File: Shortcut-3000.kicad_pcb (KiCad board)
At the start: 2 copper layers, 45 parts, among them J1 MagneticPogo_1x05_Female, J10 MagneticPogo_1x05_Female, J11 MagneticPogo_1x05_Female, J12 MagneticPogo_1x05_Female, J2 MagneticPogo_1x05_Female, J3 MagneticPogo_1x05_Female, J4 MagneticPogo_1x05_Female, J5 MagneticPogo_1x05_Female, J6 MagneticPogo_1x05_Female, J7 MagneticPogo_1x05_Female, J8 MagneticPogo_1x05_Female, J9 MagneticPogo_1x05_Female, SW1 SW_Push, SW10 SW_Push, SW11 SW_Push, SW12 SW_Push, SW13 SW_Push, SW14 SW_Push, SW15 SW_Push, SW16 RotaryEncoder_Switch, SW17 RotaryEncoder_Switch, SW2 SW_Push, SW3 SW_Push, SW4 SW_Push, SW5 SW_Push, SW6 SW_Push, SW7 SW_Push, SW8 SW_Push, SW9 SW_Push

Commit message: Switch to RP2040-Zero and route connectors through TCA9548A muxes
- Add Waveshare RP2040-Zero symbol and castellated footprint to the
  project library (dimensions from Waveshare's drawing) and replace the
  Raspberry Pi Pico with it
- Split the connectors across both I2C buses: J1-J6 on I2C0 (GP4/GP5),
  J7-J12 on I2C1 (GP6/GP7)
- Repurpose connector pin 5 as an open-drain INT line, shared per bus
  (INT0 = GP8, INT1 = GP9)
- Give each connector its own TCA9548A channel: J1-J6 on U1 ch 0-5,
  J7-J12 on U2 ch 0-5; channels 6-7 marked no-connect
- Ground mux pin 12, add 10k RESET pull-ups (R7-R8), 4.7k upstream
  pull-ups (R1-R4), 10k INT pull-ups (R5-R6) and 4.7k per-channel
  pull-ups (R9-R32)

Co-Authored-By: Claude Opus 5.5 <noreply@anthropic.com>
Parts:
- removed D1, D10, D11, D12, D13, D14, D15, D2, D3, D4, D5, D6, D7, D8, D9: 1N4148, Diode_THT:D_DO-35_SOD27_P7.62mm_Horizontal
- removed SW1, SW10, SW11, SW12, SW13, SW14, SW15, SW2, SW3, SW4, SW5, SW6, SW7, SW8, SW9: SW_Push, PCM_marbastlib-mx:SW_MX_HS_CPG151101S11_1u
- removed SW16, SW17: RotaryEncoder_Switch, Rotary_Encoder:RotaryEncoder_Alps_EC11E-Switch_Vertical_H20mm
- added R1: 4.7k, Resistor_THT:R_Axial_DIN0207_L6.3mm_D2.5mm_P7.62mm_Horizontal, F.Cu at (19.1, 22.5)
- added R10: 4.7k, Resistor_THT:R_Axial_DIN0207_L6.3mm_D2.5mm_P7.62mm_Horizontal, F.Cu at (19.1, 59.0)
- added R11: 4.7k, Resistor_THT:R_Axial_DIN0207_L6.3mm_D2.5mm_P7.62mm_Horizontal, F.Cu at (19.1, 63.0)
- added R12: 4.7k, Resistor_THT:R_Axial_DIN0207_L6.3mm_D2.5mm_P7.62mm_Horizontal, F.Cu at (29.8, 22.5)
- added R13: 4.7k, Resistor_THT:R_Axial_DIN0207_L6.3mm_D2.5mm_P7.62mm_Horizontal, F.Cu at (29.8, 26.6)
- added R14: 4.7k, Resistor_THT:R_Axial_DIN0207_L6.3mm_D2.5mm_P7.62mm_Horizontal, F.Cu at (29.8, 30.6)
- added R15: 4.7k, Resistor_THT:R_Axial_DIN0207_L6.3mm_D2.5mm_P7.62mm_Horizontal, F.Cu at (29.8, 34.7)
- added R16: 4.7k, Resistor_THT:R_Axial_DIN0207_L6.3mm_D2.5mm_P7.62mm_Horizontal, F.Cu at (29.8, 38.7)
- added R17: 4.7k, Resistor_THT:R_Axial_DIN0207_L6.3mm_D2.5mm_P7.62mm_Horizontal, F.Cu at (29.8, 42.8)
- added R18: 4.7k, Resistor_THT:R_Axial_DIN0207_L6.3mm_D2.5mm_P7.62mm_Horizontal, F.Cu at (29.8, 46.8)
- added R19: 4.7k, Resistor_THT:R_Axial_DIN0207_L6.3mm_D2.5mm_P7.62mm_Horizontal, F.Cu at (29.8, 50.9)
- added R2: 4.7k, Resistor_THT:R_Axial_DIN0207_L6.3mm_D2.5mm_P7.62mm_Horizontal, F.Cu at (19.1, 26.6)
- added R20: 4.7k, Resistor_THT:R_Axial_DIN0207_L6.3mm_D2.5mm_P7.62mm_Horizontal, F.Cu at (29.8, 54.9)
- added R21: 4.7k, Resistor_THT:R_Axial_DIN0207_L6.3mm_D2.5mm_P7.62mm_Horizontal, F.Cu at (29.8, 59.0)
- added R22: 4.7k, Resistor_THT:R_Axial_DIN0207_L6.3mm_D2.5mm_P7.62mm_Horizontal, F.Cu at (29.8, 63.0)
- added R23: 4.7k, Resistor_THT:R_Axial_DIN0207_L6.3mm_D2.5mm_P7.62mm_Horizontal, F.Cu at (40.6, 22.5)
- added R24: 4.7k, Resistor_THT:R_Axial_DIN0207_L6.3mm_D2.5mm_P7.62mm_Horizontal, F.Cu at (40.6, 26.6)
- added R25: 4.7k, Resistor_THT:R_Axial_DIN0207_L6.3mm_D2.5mm_P7.62mm_Horizontal, F.Cu at (40.6, 30.6)
- added R26: 4.7k, Resistor_THT:R_Axial_DIN0207_L6.3mm_D2.5mm_P7.62mm_Horizontal, F.Cu at (40.6, 34.7)
- added R27: 4.7k, Resistor_THT:R_Axial_DIN0207_L6.3mm_D2.5mm_P7.62mm_Horizontal, F.Cu at (40.6, 38.7)
- added R28: 4.7k, Resistor_THT:R_Axial_DIN0207_L6.3mm_D2.5mm_P7.62mm_Horizontal, F.Cu at (40.6, 42.8)
- added R29: 4.7k, Resistor_THT:R_Axial_DIN0207_L6.3mm_D2.5mm_P7.62mm_Horizontal, F.Cu at (40.6, 46.8)
- added R3: 4.7k, Resistor_THT:R_Axial_DIN0207_L6.3mm_D2.5mm_P7.62mm_Horizontal, F.Cu at (19.1, 30.6)
- added R30: 4.7k, Resistor_THT:R_Axial_DIN0207_L6.3mm_D2.5mm_P7.62mm_Horizontal, F.Cu at (40.6, 50.9)
- added R31: 4.7k, Resistor_THT:R_Axial_DIN0207_L6.3mm_D2.5mm_P7.62mm_Horizontal, F.Cu at (40.6, 54.9)
- added R32: 4.7k, Resistor_THT:R_Axial_DIN0207_L6.3mm_D2.5mm_P7.62mm_Horizontal, F.Cu at (40.6, 59.0)
- added R4: 4.7k, Resistor_THT:R_Axial_DIN0207_L6.3mm_D2.5mm_P7.62mm_Horizontal, F.Cu at (19.1, 34.7)
- added R5: 10k, Resistor_THT:R_Axial_DIN0207_L6.3mm_D2.5mm_P7.62mm_Horizontal, F.Cu at (19.1, 38.7)
- added R6: 10k, Resistor_THT:R_Axial_DIN0207_L6.3mm_D2.5mm_P7.62mm_Horizontal, F.Cu at (19.1, 42.8)
- added R7: 10k, Resistor_THT:R_Axial_DIN0207_L6.3mm_D2.5mm_P7.62mm_Horizontal, F.Cu at (19.1, 46.8)
- added R8: 10k, Resistor_THT:R_Axial_DIN0207_L6.3mm_D2.5mm_P7.62mm_Horizontal, F.Cu at (19.1, 50.9)
- added R9: 4.7k, Resistor_THT:R_Axial_DIN0207_L6.3mm_D2.5mm_P7.62mm_Horizontal, F.Cu at (19.1, 54.9)
- added U1: TCA9548APWR, Package_SO:TSSOP-24_4.4x7.8mm_P0.65mm, F.Cu at (54.6, 52.4)
- added U2: TCA9548APWR, Package_SO:TSSOP-24_4.4x7.8mm_P0.65mm, F.Cu at (63.7, 52.4)
- A1: value RaspberryPi_Pico -> RP2040-Zero; footprint Module:RaspberryPi_Pico_Common_THT -> Shortcut-3000:RP2040-Zero_Castellated
- moved A1 175.9 mm to (61.9, 33.3)
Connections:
- A1 pad 1: /COL0 -> unconnected-(A1-5V-Pad1)
- A1 pad 10: /ROW2 -> unconnected-(A1-GP13-Pad10)
- A1 pad 11: /Rotary_1_A -> unconnected-(A1-GP12-Pad11)
- A1 pad 12: /Rotary_1_B -> unconnected-(A1-GP11-Pad12)
- A1 pad 13: GND -> unconnected-(A1-GP10-Pad13)
- A1 pad 14: /Rotary_2_A -> /INT1
- A1 pad 15: /Rotary_2_B -> /INT0
- A1 pad 16: /Rotary_1_Push -> /SCL1
- A1 pad 17: /Rotary_2_Push -> /SDA1
- A1 pad 18: GND -> /SCL0
- A1 pad 19: /SDA -> /SDA0
- A1 pad 2: /COL1 -> GND
- A1 pad 20: /SCL -> unconnected-(A1-GP3-Pad20)
- A1 pad 23: GND -> unconnected-(A1-GP0-Pad23)
- A1 pad 3: GND -> +3V3
- A1 pad 4: /COL2 -> unconnected-(A1-GP29-Pad4)
- A1 pad 5: /COL3 -> unconnected-(A1-GP28-Pad5)
- A1 pad 6: /COL4 -> unconnected-(A1-GP27-Pad6)
- A1 pad 7: /ROW0 -> unconnected-(A1-GP26-Pad7)
- A1 pad 8: GND -> unconnected-(A1-GP15-Pad8)
- A1 pad 9: /ROW1 -> unconnected-(A1-GP14-Pad9)
- J1 pad 2: /SCL -> /SCL_J1
- J1 pad 4: /SDA -> /SDA_J1
- J1 pad 5: GND -> /INT0
- J10 pad 2: /SCL -> /SCL_J10
- J10 pad 4: /SDA -> /SDA_J10
- J10 pad 5: GND -> /INT1
- J11 pad 2: /SCL -> /SCL_J11
- J11 pad 4: /SDA -> /SDA_J11
- J11 pad 5: GND -> /INT1
- J12 pad 2: /SCL -> /SCL_J12
- J12 pad 4: /SDA -> /SDA_J12
- J12 pad 5: GND -> /INT1
- J2 pad 2: /SCL -> /SCL_J2
- J2 pad 4: /SDA -> /SDA_J2
- J2 pad 5: GND -> /INT0
- J3 pad 2: /SCL -> /SCL_J3
- J3 pad 4: /SDA -> /SDA_J3
- J3 pad 5: GND -> /INT0
- J4 pad 2: /SCL -> /SCL_J4
- J4 pad 4: /SDA -> /SDA_J4
- J4 pad 5: GND -> /INT0
- J5 pad 2: /SCL -> /SCL_J5
- J5 pad 4: /SDA -> /SDA_J5
- J5 pad 5: GND -> /INT0
- J6 pad 2: /SCL -> /SCL_J6
- J6 pad 4: /SDA -> /SDA_J6
- J6 pad 5: GND -> /INT0
- J7 pad 2: /SCL -> /SCL_J7
- J7 pad 4: /SDA -> /SDA_J7
- J7 pad 5: GND -> /INT1
- J8 pad 2: /SCL -> /SCL_J8
- J8 pad 4: /SDA -> /SDA_J8
- J8 pad 5: GND -> /INT1
- J9 pad 2: /SCL -> /SCL_J9
- J9 pad 4: /SDA -> /SDA_J9
- J9 pad 5: GND -> /INT1

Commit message: Backup before removing PCB routing
Co-Authored-By: Claude Opus 5.5 <noreply@anthropic.com>
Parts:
- A1, U1, U2: moved to B.Cu
- R1, R10, R11, R12, R13, R14, R15, R16, R17, R18, R19, R2, R20, R21, R22, R23, R24, R25, R26, R27, R28, R29, R3, R30, R31, R32, R4, R5, R6, R7, R8, R9: footprint Resistor_THT:R_Axial_DIN0207_L6.3mm_D2.5mm_P7.62mm_Horizontal -> Resistor_SMD:R_0805_2012Metric; moved to B.Cu
- moved R8 158.6 mm to (176.3, 71.2), turned to -90 degrees
- moved R7 156.2 mm to (173.4, 71.2), turned to -90 degrees
- moved R6 154.0 mm to (170.4, 71.2), turned to -90 degrees
- moved J10 152.3 mm to (158.8, 102.7)
- moved J11 152.3 mm to (184.2, 102.7)
- moved J2 152.3 mm to (158.8, 51.9)
- moved J3 152.3 mm to (184.2, 51.9)
- moved J6 152.3 mm to (158.8, 77.3)
- moved J7 152.3 mm to (184.2, 77.3)
- moved J1 152.3 mm to (133.4, 51.9)
- moved J12 152.3 mm to (209.6, 102.7)
- moved J4 152.3 mm to (209.6, 51.9)
- moved J5 152.3 mm to (133.4, 77.3)
- moved J8 152.3 mm to (209.6, 77.3)
- moved J9 152.3 mm to (133.4, 102.7)
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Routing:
- net GND: track 0.00 -> 417.4 mm
- net +3V3: track 0.00 -> 405.8 mm, vias 0 -> 1
- net /INT1: track 0.00 -> 157.5 mm, vias 0 -> 3
- net /SCL_J12: track 0.00 -> 63.4 mm, vias 0 -> 1
- net /SCL_J11: track 0.00 -> 57.2 mm, vias 0 -> 1
- net /SDA_J12: track 0.00 -> 52.7 mm, vias 0 -> 1
- net /SDA_J11: track 0.00 -> 41.2 mm, vias 0 -> 1
- net /INT0: track 0.00 -> 38.6 mm
- net /SCL_J7: track 0.00 -> 32.6 mm, vias 0 -> 1
- net /SDA_J8: track 0.00 -> 30.6 mm
- net /SCL_J8: track 0.00 -> 26.9 mm
- net /SDA_J7: track 0.00 -> 22.7 mm, vias 0 -> 1
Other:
- board outline added: 105.5 x 82.5 mm

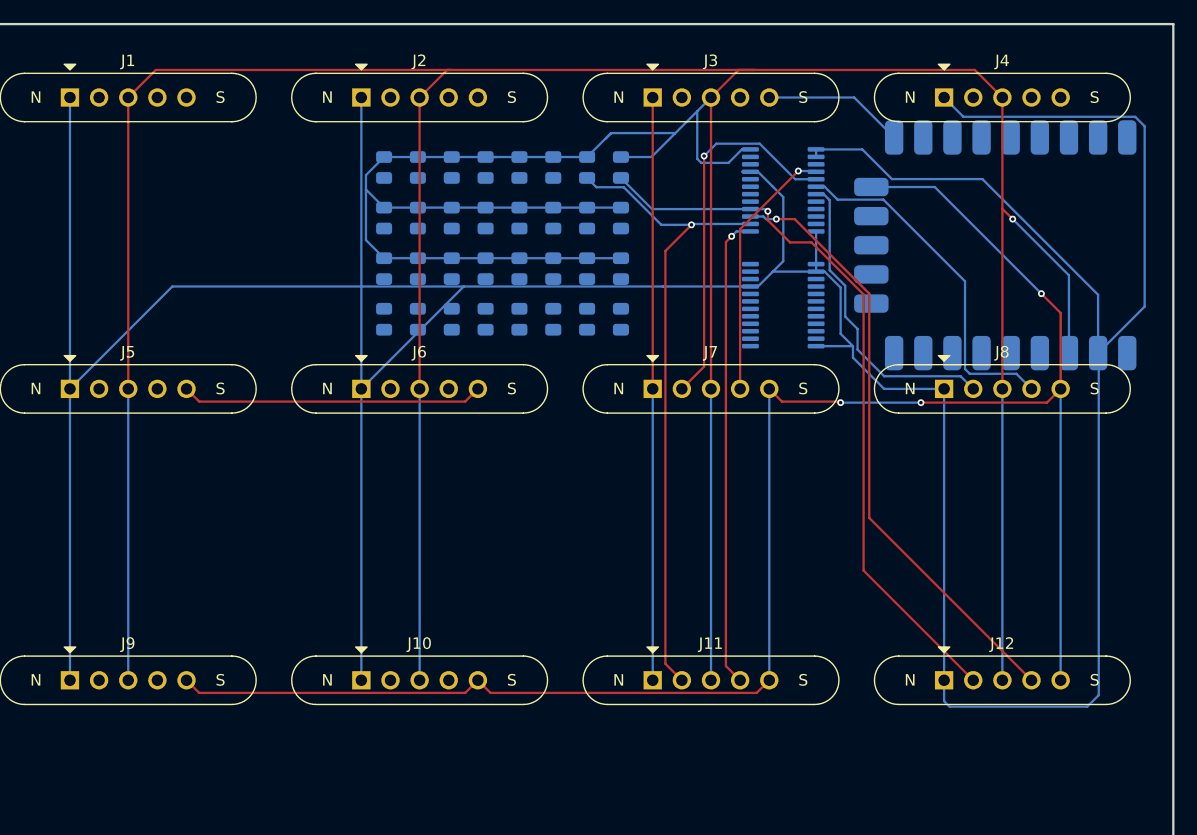
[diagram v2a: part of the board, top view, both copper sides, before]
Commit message: Backup before replacing 3V3 routing with fill
Co-Authored-By: Claude Opus 5.5 <noreply@anthropic.com>
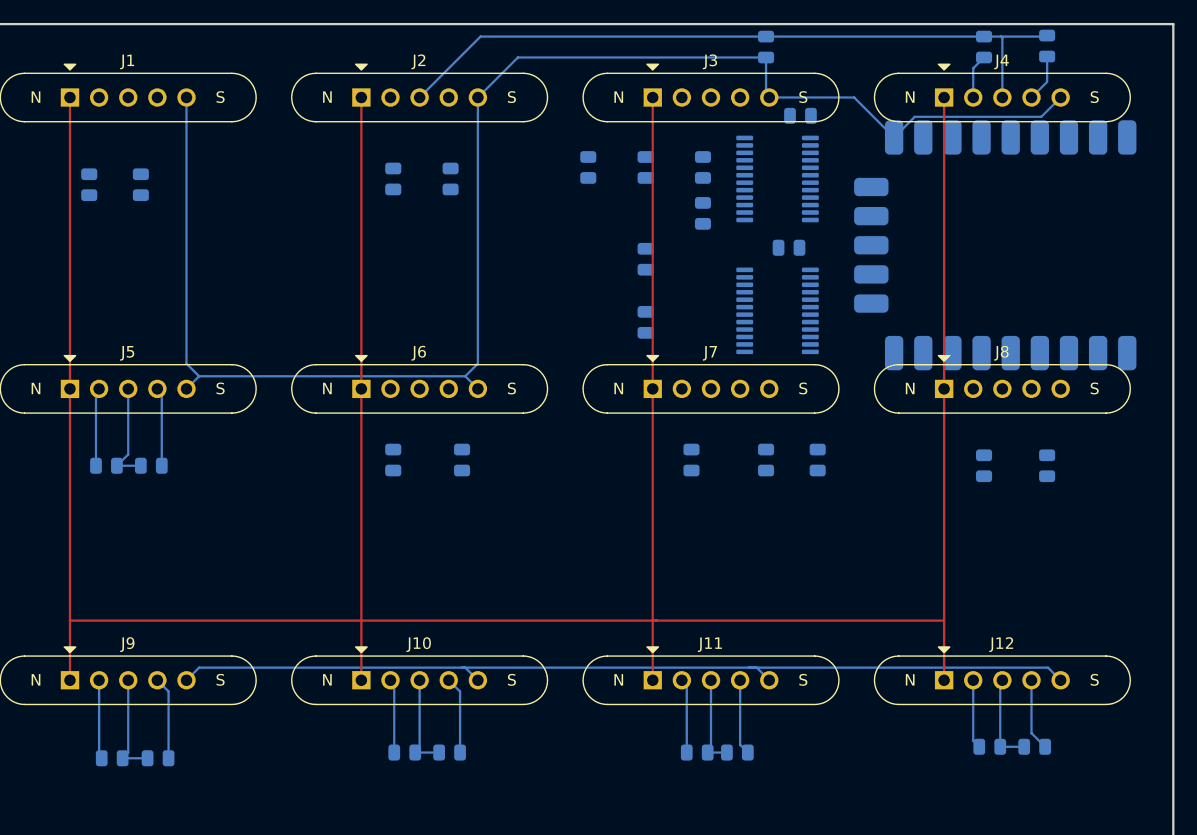
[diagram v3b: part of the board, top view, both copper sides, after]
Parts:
- moved R20 66.4 mm to (212.4, 108.5), turned to 0 degrees
- moved R29 62.5 mm to (132.0, 109.5), turned to 180 degrees
- moved R32 59.9 mm to (208.5, 108.5), turned to 180 degrees
- moved R19 52.8 mm to (186.5, 109.0), turned to 0 degrees
- moved R12 52.7 mm to (213.5, 47.4)
- moved R30 52.6 mm to (157.5, 109.0), turned to 180 degrees
- moved R31 51.9 mm to (183.0, 109.0), turned to 180 degrees
- moved R17 51.0 mm to (136.0, 109.5), turned to 0 degrees
- moved R28 50.6 mm to (208.0, 84.0)
- moved R18 46.7 mm to (161.4, 109.0), turned to 0 degrees
- moved R16 40.9 mm to (213.5, 84.0)
- moved R21 37.6 mm to (130.0, 59.5)
- moved R13 36.4 mm to (135.4, 84.0), turned to 0 degrees
- moved R25 35.5 mm to (131.5, 84.0), turned to 180 degrees
- moved R24 35.0 mm to (208.0, 47.5)
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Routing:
- net +3V3: track 405.8 -> 105.9 mm, vias 1 -> 0
- net GND: track 417.4 -> 279.8 mm
- net /INT0: track 38.6 -> 134.3 mm
- net /INT1: track 157.5 -> 81.2 mm, vias 3 -> 0
- net /SCL_J12: track 63.4 -> 6.02 mm, vias 1 -> 0
- net /SCL_J11: track 57.2 -> 6.48 mm, vias 1 -> 0
- net /SDA_J12: track 52.7 -> 6.29 mm, vias 1 -> 0
- net /SDA_J11: track 41.2 -> 6.58 mm, vias 1 -> 0
- net /SCL_J7: track 32.6 -> 0.00 mm, vias 1 -> 0
- net /SDA_J8: track 30.6 -> 0.00 mm
- net /SCL_J8: track 26.9 -> 0.00 mm
- net /SDA_J7: track 22.7 -> 0.00 mm, vias 1 -> 0
- net /SDA_J9: track 0.00 -> 7.20 mm
- net /SCL_J9: track 0.00 -> 6.89 mm
- net /SDA_J5: track 0.00 -> 6.86 mm
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
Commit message: Replace 3V3 routing with B.Cu 3V3 fill zone
Co-Authored-By: Claude Opus 5.5 <noreply@anthropic.com>
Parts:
- moved R11 10.3 mm to (173.5, 67.0), turned to 90 degrees
- moved U1 4.00 mm to (186.0, 70.5)
- moved R7 2.06 mm to (191.5, 67.0), turned to -90 degrees
- moved R12 1.50 mm to (213.5, 48.9)
- moved R24 1.50 mm to (208.0, 49.0)
- moved R1 1.00 mm to (178.5, 67.0)
- moved R2 1.00 mm to (178.5, 70.5)
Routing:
- net +3V3: track 105.9 -> 1.09 mm
- net /SCL_J1: track 0.00 -> 100.6 mm, vias 0 -> 1
- net /SDA_J1: track 0.00 -> 94.0 mm, vias 0 -> 1
- net /SCL_J2: track 0.00 -> 73.3 mm, vias 0 -> 1
- net /SDA_J3: track 0.00 -> 70.6 mm
- net /SCL_J5: track 6.81 -> 73.9 mm
- net /INT1: track 81.2 -> 145.9 mm
- net /SDA_J5: track 6.86 -> 69.7 mm, vias 0 -> 2
- net /SCL_J3: track 0.00 -> 47.7 mm
- net /SCL_J6: track 0.00 -> 45.7 mm, vias 0 -> 1
- net GND: track 279.8 -> 324.7 mm, vias 0 -> 2
- net /SDA_J4: track 4.14 -> 48.5 mm
- net /SDA_J2: track 0.00 -> 41.1 mm
- net /SDA_J6: track 0.00 -> 38.1 mm
- net /INT0: track 134.3 -> 172.3 mm
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- added copper zone on B.Cu, net +3V3

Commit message: Backup before changing pogo pin hole size
Co-Authored-By: Claude Opus 5.5 <noreply@anthropic.com>
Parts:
- moved R8 44.0 mm to (179.0, 95.5)
- moved R3 38.1 mm to (194.5, 94.5)
- moved U2 33.7 mm to (186.0, 92.4), turned to 0 degrees
- moved R4 30.5 mm to (194.5, 90.5)
- moved R2 1.50 mm to (177.0, 70.5)
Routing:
- net /SDA1: track 0.00 -> 84.4 mm, vias 0 -> 2
- net /SCL_J11: track 6.48 -> 88.7 mm
- net /SCL_J9: track 6.89 -> 64.1 mm
- net /SCL1: track 0.00 -> 54.3 mm, vias 0 -> 4
- net /SDA_J9: track 7.20 -> 59.1 mm
- net +3V3: track 1.09 -> 43.9 mm, vias 0 -> 8
- net /SDA_J12: track 6.29 -> 48.4 mm
- net /SDA0: track 4.78 -> 44.8 mm, vias 0 -> 2
- net /SDA_J8: track 8.18 -> 43.3 mm, vias 0 -> 2
- net /SCL_J10: track 6.44 -> 41.3 mm, vias 0 -> 1
- net /SCL_J8: track 8.05 -> 38.8 mm, vias 0 -> 2
- net /INT0: track 172.3 -> 143.2 mm, vias 0 -> 2
- net /SDA_J10: track 6.71 -> 35.6 mm, vias 0 -> 1
- net /INT1: track 145.9 -> 172.8 mm
- net /SCL_J12: track 6.02 -> 32.0 mm, vias 0 -> 1
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
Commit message: Change pogo pin hole size and add 4-pin magnetic pogo footprints
Co-Authored-By: Claude Opus 5.5 <noreply@anthropic.com>
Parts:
- moved R5 10.4 mm to (192.0, 57.5), turned to 90 degrees
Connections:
- A1 pad 1: unconnected-(A1-5V-Pad1) -> +5V
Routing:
- net /INT0: track 143.2 -> 149.0 mm
